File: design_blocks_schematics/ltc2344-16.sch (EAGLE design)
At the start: 6 parts

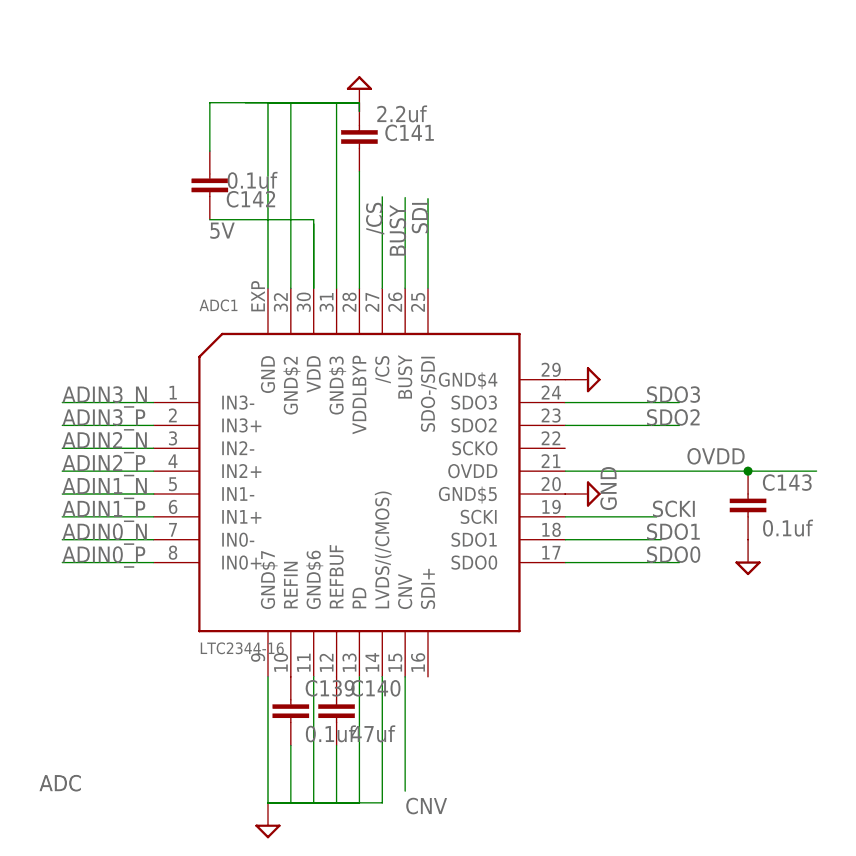
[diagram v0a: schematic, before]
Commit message: cleaned up schematic of ADC
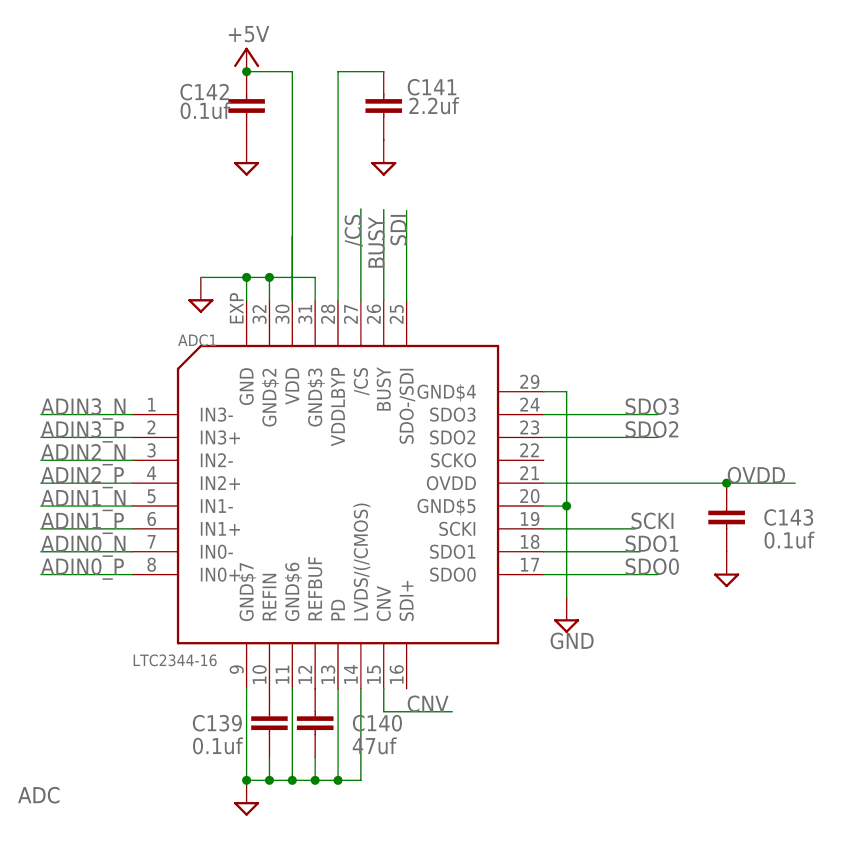
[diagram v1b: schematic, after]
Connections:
- net 5V renamed +5V
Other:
- moved on the sheet: ADC1, C139, C140, C141, C142, C143
